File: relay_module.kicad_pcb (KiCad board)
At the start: 2 copper layers, 45.7 x 36.8 mm, 14 parts, among them J1 Screw_Terminal_1x02, J2 Screw_Terminal_1x02, J3 Screw_Terminal_1x03, Q1 Q_NMOS_DGS

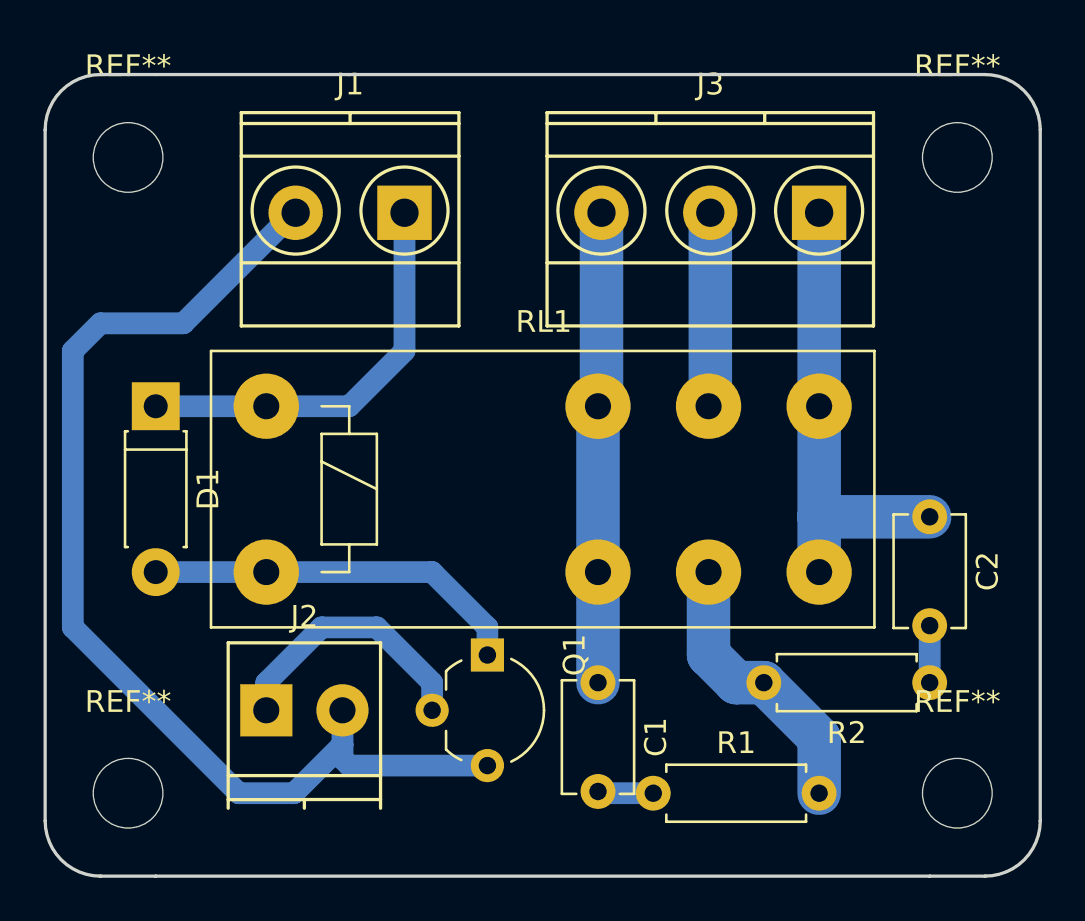
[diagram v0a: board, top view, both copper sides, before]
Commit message: add pull-down resistor for transitor
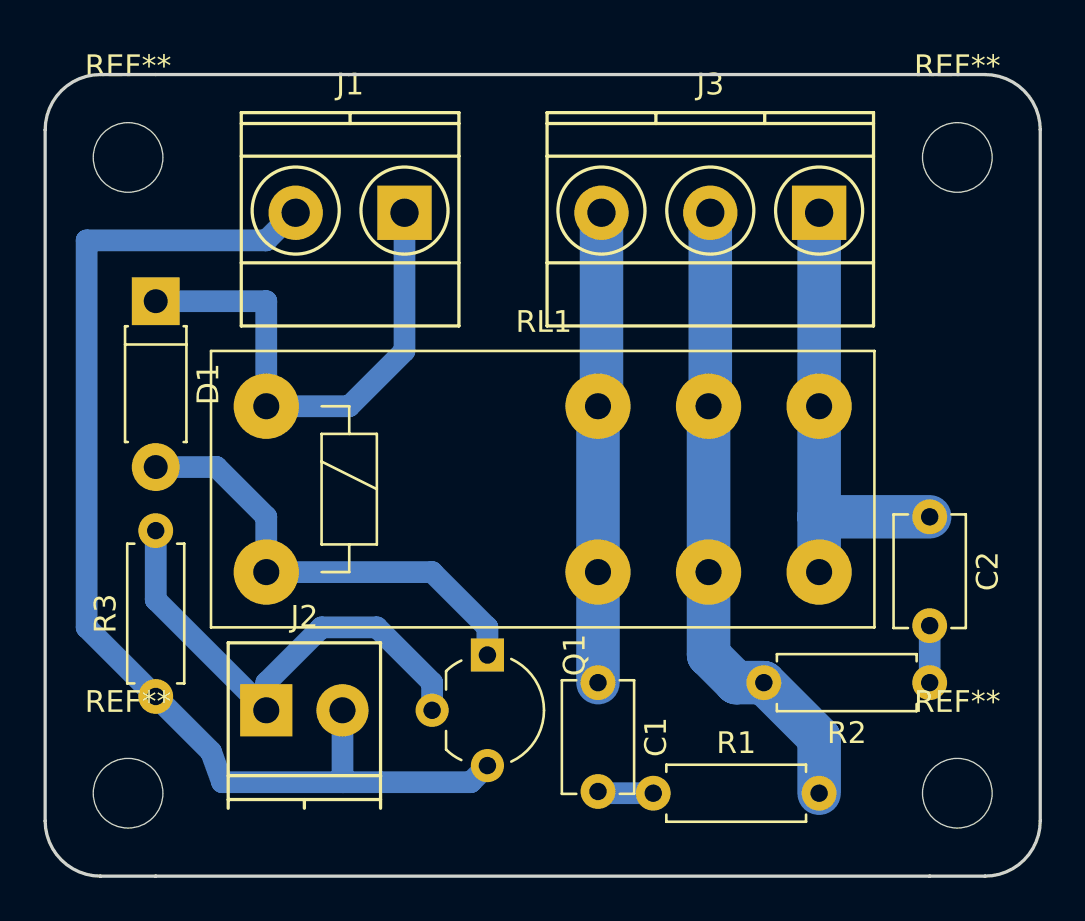
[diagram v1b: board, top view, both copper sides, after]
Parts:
- added R3: R, Resistors_THT:R_Axial_DIN0207_L6.3mm_D2.5mm_P7.62mm_Horizontal, F.Cu at (146.1, 95.9)
- moved D1 4.83 mm to (146.1, 77.7)
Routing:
- net Net-(J2-Pad1): track 12.3 -> 22.6 mm
- net Net-(J3-Pad2): track 21.9 -> 29.6 mm
- net Net-(D1-Pad1): track 18.8 -> 23.7 mm
- net Net-(D1-Pad2): track 17.6 -> 21.0 mm
- net Net-(J1-Pad2): track 51.1 -> 53.5 mm
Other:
- net class Default: clearance 0.8 -> 1
- rule trace_clearance: 0.8 -> 1
